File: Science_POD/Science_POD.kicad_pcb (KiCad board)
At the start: 2 copper layers, 38.1 x 59.9 mm, 14 parts, among them U1 Molex_SL_2, U2 AP1059, U3 ESP_8266_Breakout_Small, U4 Molex_SL_3, U5 Molex_SL_3

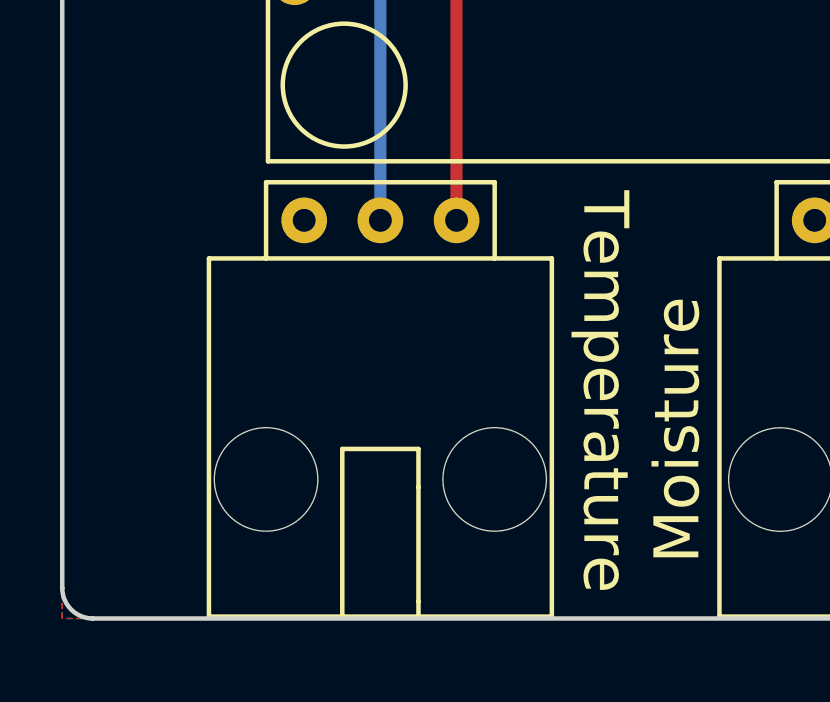
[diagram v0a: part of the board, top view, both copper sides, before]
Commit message: Chenged thermister back to SL-2
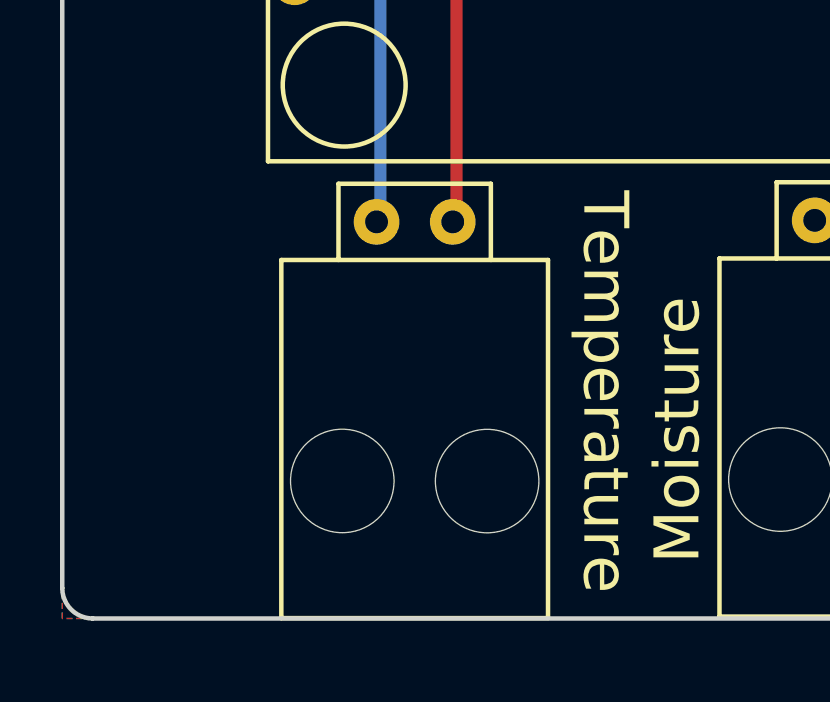
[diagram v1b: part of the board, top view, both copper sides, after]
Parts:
- removed U5: Molex_SL_3, MRDT_Connectors:MOLEX_SL_3_Horizontal
- added Conn1: Molex_SL_2, MRDT_Connectors:MOLEX_SL_2_Horizontal, F.Cu at (176.8, 128.5)
- R1: value 10K -> 4.7K
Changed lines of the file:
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@@
 (kicad_pcb (version 4) (host pcbnew 4.0.7)
   (general
-    (links 28)
+    (links 27)
     (no_connects 0)
-    (area 165.024999 80.369999 203.275001 141.943501)
+    (area 165.024999 81.712999 203.275001 141.807001)
     (thickness 1.6)
-    (drawings 20)
+    (drawings 19)
     (tracks 51)
     (zones 0)
@@
       (effects (font (size 1 1) (thickness 0.15)))
     )
-    (fp_text value 10K (at 0 1.55 90) (layer F.Fab)
+    (fp_text value 4.7K (at 0 1.55 90) (layer F.Fab)
       (effects (font (size 1 1) (thickness 0.15)))
     )
@@
     )
   )
-  (module MRDT_Connectors:MOLEX_SL_3_Horizontal (layer F.Cu)
-    (at 175.7045 128.4605 180)
-    (fp_text reference U5 (at -1.27 2.54 180) (layer F.SilkS) hide
-      (effects (font (size 1 1) (thickness 0.15)))
-    )
-    (fp_text value Molex_SL_3 (at 0.635 2.032 180) (layer F.Fab)
-      (effects (font (size 1 1) (thickness 0.15)))
-    )
-    (fp_line (start 1.27 -7.62) (end -1.27 -7.62) (layer F.SilkS) (width 0.15))
-    (fp_line (start 5.715 -13.208) (end -5.715 -13.208) (layer F.SilkS) (width 0.15))
-    (fp_line (start 5.715 -1.27) (end -3.81 -1.27) (layer F.SilkS) (width 0.15))
-    (fp_line (start 3.81 1.27) (end -3.81 1.27) (layer F.SilkS) (width 0.15))
-    (fp_line (start 1.27 -13.208) (end 1.27 -7.62) (layer F.SilkS) (width 0.15))
-    (fp_line (start 5.715 -1.27) (end 5.715 -13.208) (layer F.SilkS) (width 0.15))
-    (fp_line (start -1.27 -13.208) (end -1.27 -12.7) (layer F.SilkS) (width 0.15))
-    (fp_line (start -5.715 -1.27) (end -5.715 -13.208) (layer F.SilkS) (width 0.15))
-    (fp_line (start -3.81 -1.27) (end -5.715 -1.27) (layer F.SilkS) (width 0.15))
-    (fp_line (start -1.27 -8.89) (end -1.27 -7.62) (layer F.SilkS) (width 0.15))
-    (fp_line (start -1.27 -8.89) (end -1.27 -12.7) (layer F.SilkS) (width 0.15))
-    (fp_line (start 3.81 -1.27) (end 3.81 1.27) (layer F.SilkS) (width 0.15))
-    (fp_line (start -3.81 1.27) (end -3.81 -1.27) (layer F.SilkS) (width 0.15))
-    (pad 1 thru_hole circle (at -2.54 0 180) (size 1.524 1.524) (drill 0.762) (layers *.Cu *.Mask)
+  (module MRDT_Connectors:MOLEX_SL_2_Horizontal (layer F.Cu)
+    (at 176.8475 128.5113 180)
+    (fp_text reference Conn1 (at 0 2.54 180) (layer F.SilkS) hide
+      (effects (font (size 1 1) (thickness 0.15)))
+    )
+    (fp_text value Molex_SL_2 (at 1.27 2.286 180) (layer F.Fab)
+      (effects (font (size 1 1) (thickness 0.15)))
+    )
+    (fp_line (start -4.445 -1.27) (end 4.445 -1.27) (layer F.SilkS) (width 0.15))
+    (fp_line (start 4.445 -1.27) (end 4.445 -13.208) (layer F.SilkS) (width 0.15))
+    (fp_line (start 2.54 1.27) (end -2.54 1.27) (layer F.SilkS) (width 0.15))
+    (fp_line (start -4.445 -13.208) (end 4.445 -13.208) (layer F.SilkS) (width 0.15))
+    (fp_line (start -4.445 -1.27) (end -4.445 -13.208) (layer F.SilkS) (width 0.15))
+    (fp_line (start 2.54 -1.27) (end 2.54 1.27) (layer F.SilkS) (width 0.15))
+    (fp_line (start -2.54 1.27) (end -2.54 -1.27) (layer F.SilkS) (width 0.15))
+    (pad "" np_thru_hole circle (at -2.415 -8.64 180) (size 3.45 3.45) (drill 3.45) (layers *.Cu *.Mask))
+    (pad 1 thru_hole circle (at -1.27 0 180) (size 1.524 1.524) (drill 0.762) (layers *.Cu *.Mask)
       (net 4 /Ain))
-    (pad 2 thru_hole circle (at 0 0 180) (size 1.524 1.524) (drill 0.762) (layers *.Cu *.Mask)
+    (pad 2 thru_hole circle (at 1.27 0 180) (size 1.524 1.524) (drill 0.762) (layers *.Cu *.Mask)
       (net 5 /D1))
-    (pad 3 thru_hole circle (at 2.54 0 180) (size 1.524 1.524) (drill 0.762) (layers *.Cu *.Mask)
-      (net 6 /GND))
-    (pad "" np_thru_hole circle (at -3.81 -8.636 180) (size 3.45 3.45) (drill 3.45) (layers *.Cu *.Mask))
-    (pad "" np_thru_hole circle (at 3.81 -8.636 180) (size 3.45 3.45) (drill 3.45) (layers *.Cu *.Mask))
-  )
-  (gr_text - (at 173.1645 131.3815) (layer B.SilkS)
+    (pad "" np_thru_hole circle (at 2.413 -8.636 180) (size 3.45 3.45) (drill 3.45) (layers *.Cu *.Mask))
+  )
+  (gr_text - (at 175.7045 130.3909) (layer B.SilkS)
     (effects (font (size 1.5 1.5) (thickness 0.3)) (justify mirror))
   )
-  (gr_text + (at 175.7045 131.3815) (layer B.SilkS)
-    (effects (font (size 1.5 1.5) (thickness 0.3)) (justify mirror))
-  )

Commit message: Buck Converter had incorrect value
Corrected to AP1509.
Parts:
- U2: value AP1059 -> AP1509
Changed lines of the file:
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@@
     (links 27)
     (no_connects 0)
-    (area 165.024999 81.712999 203.275001 141.807001)
+    (area 165.024999 80.369999 203.275001 141.994301)
     (thickness 1.6)
     (drawings 19)
@@
       (effects (font (size 1 1) (thickness 0.15)))
     )
-    (fp_text value AP1059 (at 0 3.5) (layer F.Fab)
-      (effects (font (size 1 1) (thickness 0.15)))
-    )
+    (fp_text value AP1509 (at 0 3.5) (layer F.Fab)
+      (effects (font (size 1 1) (thickness 0.15)))
+    )
